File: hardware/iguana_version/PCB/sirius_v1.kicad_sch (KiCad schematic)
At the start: 115 parts, among them J1 BAT, J10 OLED, J12 USB_B_Micro, J13 HDR-2x1, J14 Conn_01x02, J17 Conn_Coaxial, J18 IN, J19 IN, J2 HDR-2x1, J3 IN, J4 Cap. Moisture Sensor, J5 ds18b20, J6 SHT31, J7 NPK/H Sensor, J8 ON OFF, J9 HDR-3x1, Q1 Q_PMOS_GSD, Q10 BSS138, Q2 Q_PMOS_GSD, Q3 Q_Dual_NPN_NPN_BRT_E1B1C2E2B2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, Q4 BSS138, Q6 Q_PMOS_GSD, Q7 Q_PMOS_GSD, Q9 BSS138, SW1 SW_DIP_x02, SW2 SW_DIP_x02, SW3 SW_DIP_x02, U1 DW01, U10 ESP32-WROOM-32D, U11 RV-8803, U12 RFM95W-915S2, U2 TP4056, U3 MT3608, U4 FS8205A, U5 AP2112K-3.3, U6 AP2112K-3.3, U8 AP2112K-3.3, U9 CH340C

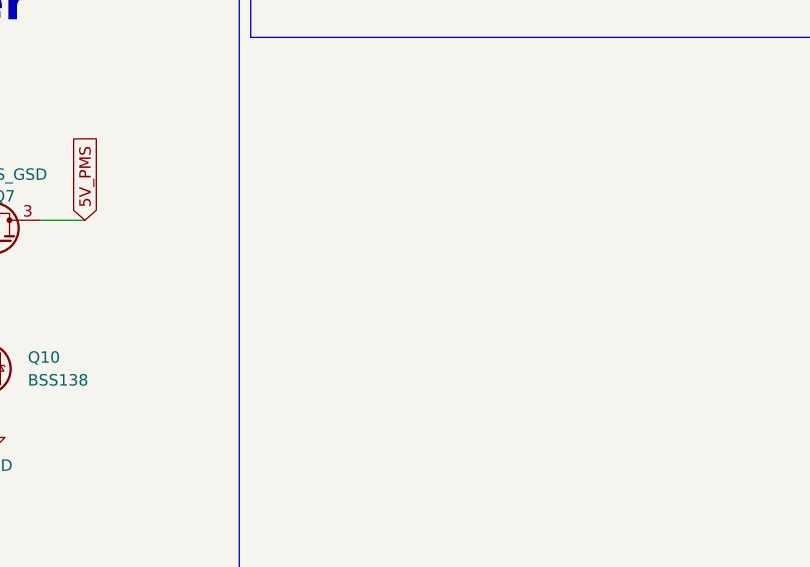
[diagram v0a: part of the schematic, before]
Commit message: code updating upto node 12 and add sensor AHT10 capabilities
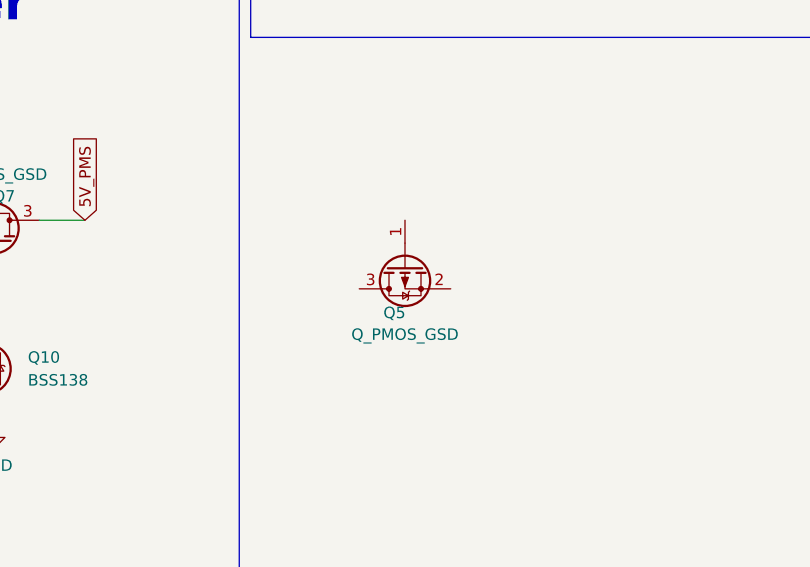
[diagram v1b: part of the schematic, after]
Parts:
- added Q5: Q_PMOS_GSD, Package_TO_SOT_SMD:SOT-23, symbol Device:Q_PMOS_GSD
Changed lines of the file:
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@@
+	)
+	(symbol
+		(lib_id "Device:Q_PMOS_GSD")
+		(at 266.7 300.99 90)
+		(mirror x)
+		(unit 1)
+		(exclude_from_sim no)
+		(in_bom yes)
+		(on_board yes)
+		(dnp no)
+		(property "Reference" "Q5"
+			(at 265.5316 306.197 90)
+			(effects
+				(font
+					(size 1.27 1.27)
+				)
+			)
+		)
+		(property "Value" "Q_PMOS_GSD"
+			(at 266.7 308.61 90)
+			(effects
+				(font
+					(size 1.27 1.27)
+				)
+			)
+		)
+		(property "Footprint" "Package_TO_SOT_SMD:SOT-23"
+			(at 264.16 306.07 0)
+			(effects
+				(font
+					(size 1.27 1.27)
+				)
+				(hide yes)
+			)
+		)
+		(property "Datasheet" "~"
+			(at 266.7 300.99 0)
+			(effects
+				(font
+					(size 1.27 1.27)
+				)
+				(hide yes)
+			)
+		)
+		(property "Description" ""
+			(at 266.7 300.99 0)
+			(effects
+				(font
+					(size 1.27 1.27)
+				)
+				(hide yes)
+			)
+		)
+		(pin "1"
+		)
+		(pin "2"
+		)
+		(pin "3"
+		)
+		(instances
+			(project "sirius_v1"
+				(path "/3b57faab-ddb3-4ef8-883c-40a3ac2704ad"
+					(reference "Q5")
+					(unit 1)
+				)
+			)
+		)
 	)
 	(symbol

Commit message: updating fab files
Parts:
- removed J8: ON OFF, Jumper:SolderJumper-2_P1.3mm_Open_RoundedPad1.0x1.5mm, symbol IoWLabsConnectors:HDR-2x1
- removed Q5: Q_PMOS_GSD, Package_TO_SOT_SMD:SOT-23, symbol Device:Q_PMOS_GSD
- added JP4, JP5: SolderJumper_2_Open, Jumper:SolderJumper-2_P1.3mm_Open_RoundedPad1.0x1.5mm, symbol Jumper:SolderJumper_2_Open
- C1, C2, C5, D12, D3, D4, D5, D6, D7, L1, R10, R11, R12, R2, R23, R4, R5, R6, R8, SW1, U1, U3, U4: now not fitted
- C3, C4, D1, D2, R1, R3, U2: DNP (none) -> DNP; now not fitted
- R35, R36: value 10K -> 330
- R39, R40: value 10K -> 0
- R7: value 12K -> 12k
- R9: value 30K -> 3.3k
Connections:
- net +5V: now also JP5.1 (A)
- net Vin_main: now also JP4.1 (A)
- net Vo_DCDC: now also JP4.2 (B), JP5.2 (B)
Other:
- note added: "Jumper. to avoid battery circuit"
- note added: "ON/OFF jumper"
- note added: "PWR control"
- note removed: "RS485 converter"
- moved on the sheet: J2

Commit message: changes on bom
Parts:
- D5, D6, D7, R10, R11, R12: now fitted
